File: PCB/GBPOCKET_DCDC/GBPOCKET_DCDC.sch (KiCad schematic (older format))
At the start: 23 parts, among them J1 Conn_01x03, J2 Conn_01x02, U1 MCP1623, U2 MAX868

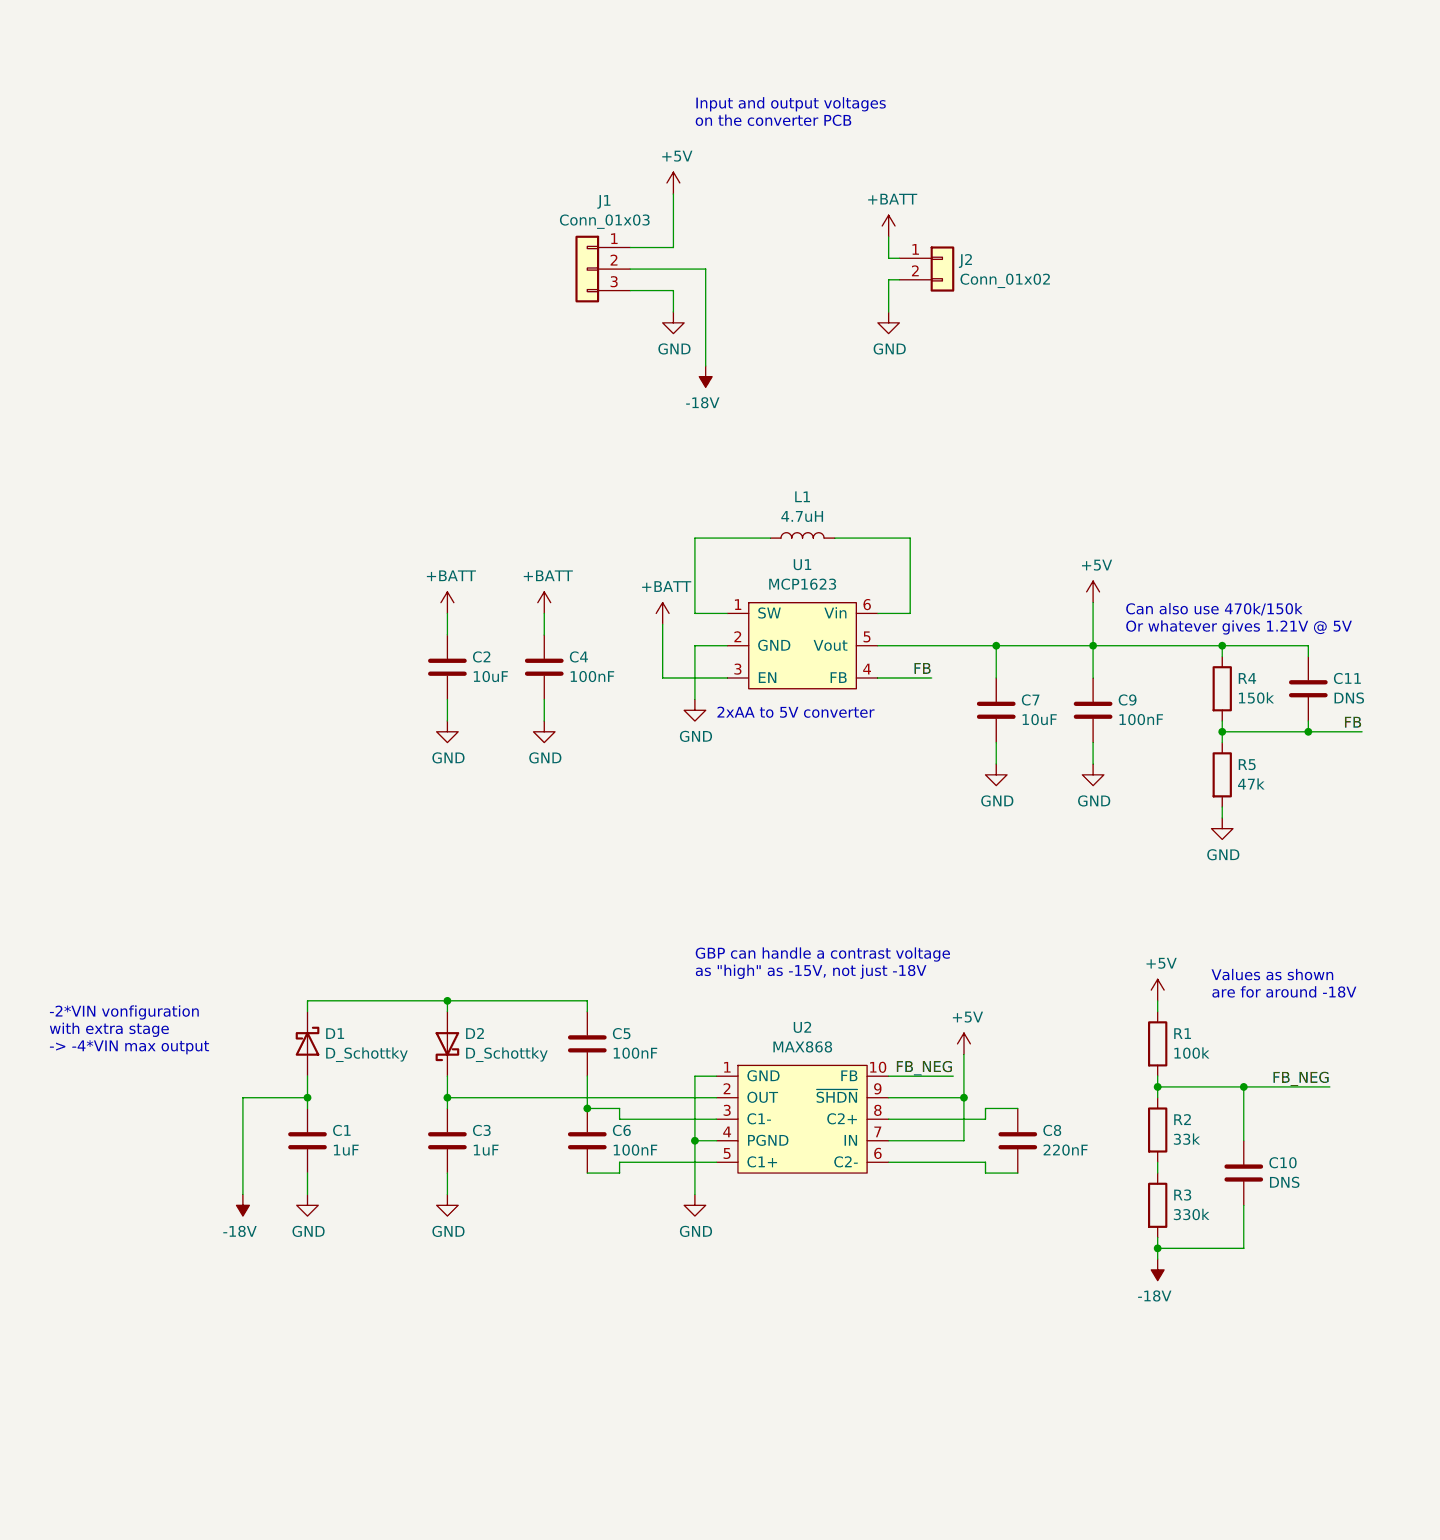
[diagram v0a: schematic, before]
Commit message: Updated schematic a bit Added header for LED Finished PCB (quick'n'dirty, bit it'll do) Exported gerbers for production
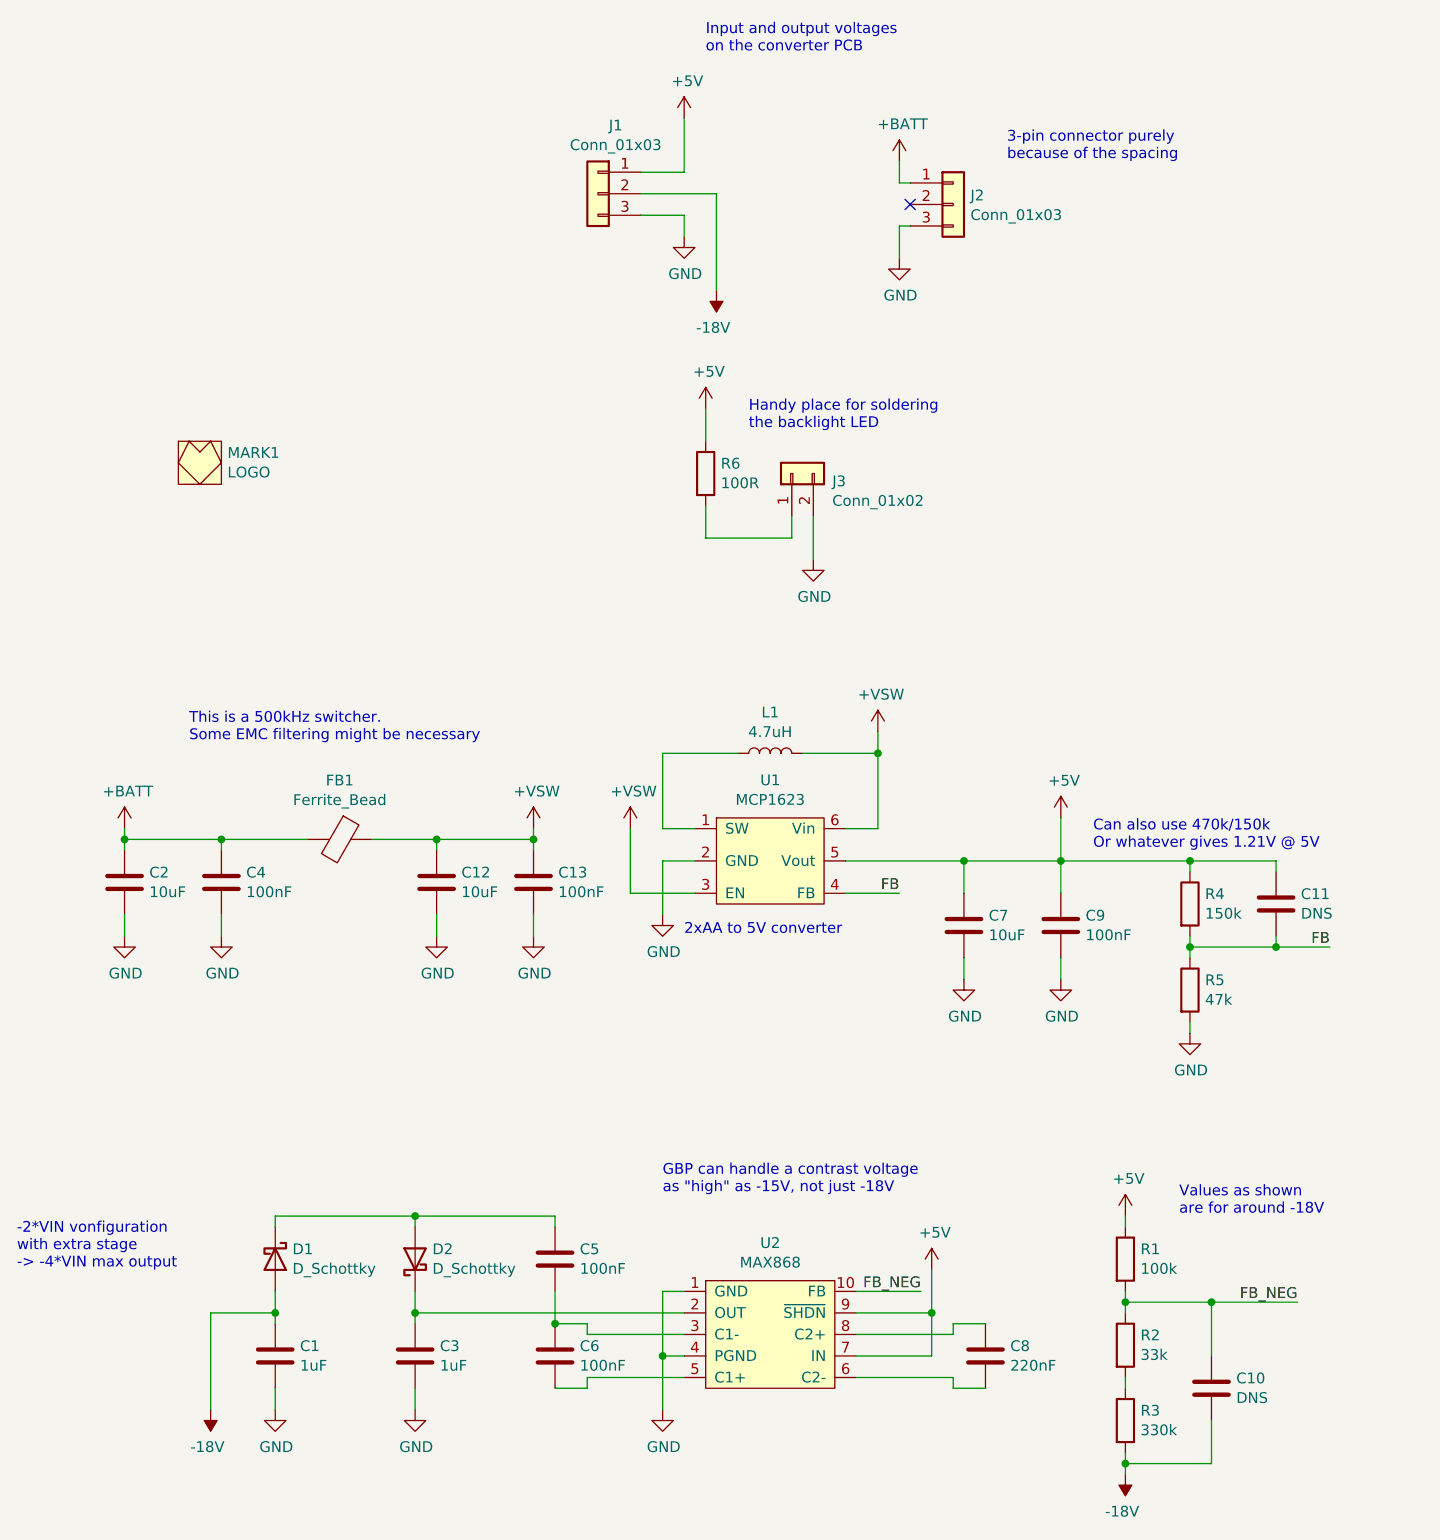
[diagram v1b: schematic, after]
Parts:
- removed J2: Conn_01x02, Connector_PinHeader_2.54mm:PinHeader_1x02_P2.54mm_Vertical, symbol Connector_Generic:Conn_01x02
- added C12: 10uF, Capacitor_SMD:C_0805_2012Metric_Pad1.18x1.45mm_HandSolder, symbol Device:C
- added C13: 100nF, Capacitor_SMD:C_0603_1608Metric_Pad1.08x0.95mm_HandSolder, symbol Device:C
- added FB1: Ferrite_Bead, Inductor_SMD:L_0805_2012Metric_Pad1.15x1.40mm_HandSolder, symbol Device:Ferrite_Bead
- added J2: Conn_01x03, Connector_PinHeader_2.54mm:PinHeader_1x03_P2.54mm_Vertical, symbol Connector_Generic:Conn_01x03
- added J3: Conn_01x02, Connector_PinHeader_2.54mm:PinHeader_1x02_P2.54mm_Vertical, symbol Connector_Generic:Conn_01x02
- added MARK1: LOGO, Kicad_Library:FOX_LOGO_SILK, symbol Kicad_Library:LOGO
- added R6: 100R, Resistor_SMD:R_0603_1608Metric_Pad0.98x0.95mm_HandSolder, symbol Device:R
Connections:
- net +5V: now also R6.1
- net +BATT: now also FB1.2, J2.1 (Pin_1); no longer U1.3 (EN)
- net GND: now also C12.2, C13.2, J2.3 (Pin_3), J3.2 (Pin_2)
- net +VSW: now reaches L1.2, U1.6 (Vin)
- net +VSW: now also U1.3 (EN), C12.1, C13.1, FB1.1
- new net: J3.1 (Pin_1), R6.2
- no-connect marks 0 -> 1
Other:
- note added: "3-pin connector purely\nbecause of the spacing"
- note added: "Handy place for soldering\nthe backlight LED"
- note added: "This is a 500kHz switcher.\nSome EMC filtering might be necessary"
- moved on the sheet: C1, C10, C11, C2, C3, C4, C5, C6, C7, C8, C9, D1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
